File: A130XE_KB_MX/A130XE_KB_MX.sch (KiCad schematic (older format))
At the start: 77 parts, among them J1 34 pin RIBBON KEYBOARD CABLE, J2 Conn_01x02_Male, J3 Conn_01x03_Male, J4 Conn_01x03_Male, SW1 KS_RESET, SW10 K_5, SW11 K_I, SW12 K_T, SW13 K_G, SW14 K_SPACE, SW15 K_B, SW16 K_K, SW17 KS_SELECT, SW18 K_4, SW19 K_O, SW2 K_6, SW20 K_R, SW21 K_F, SW22 K_M, SW23 K_V, SW24 K_L, SW25 K_3, SW26 K_P, SW27 K_E, SW28 K_D, SW29 KS_START, SW3 K_U, SW30 K_comma, SW31 K_comdot, SW32 K_C, SW33 K_dot, SW34 K_2, SW35 K_minus, SW36 K_W, SW37 K_S, SW38 K_X, SW39 K_plus, SW4 K_Y, SW40 K_1, SW41 K_equal, SW42 K_Q, SW43 K_A, SW44 K_slash, SW45 K_asterisk, SW46 K_Z, SW47 K_ATARI, SW48 K_ESC, SW49 K_RETURN, SW5 K_H, SW50 K_TAB, SW51 K_CAPS, SW52 K_CTRL, SW53 K_LSHIFT, SW54 K_RSHIFT, SW55 K_BRK, SW56 K_DEL, SW57 K_GT, SW58 K_LT, SW59 K_0, SW6 K_N, SW60 K_9, SW61 K_8, SW62 K_7, SW63 K_SPACE_1, SW64 K_SPACE_2, SW65 K_F1, SW66 K_F2, SW67 K_F3, SW68 K_F4, SW7 KS_HELP, SW8 K_J, SW9 KS_OPTION

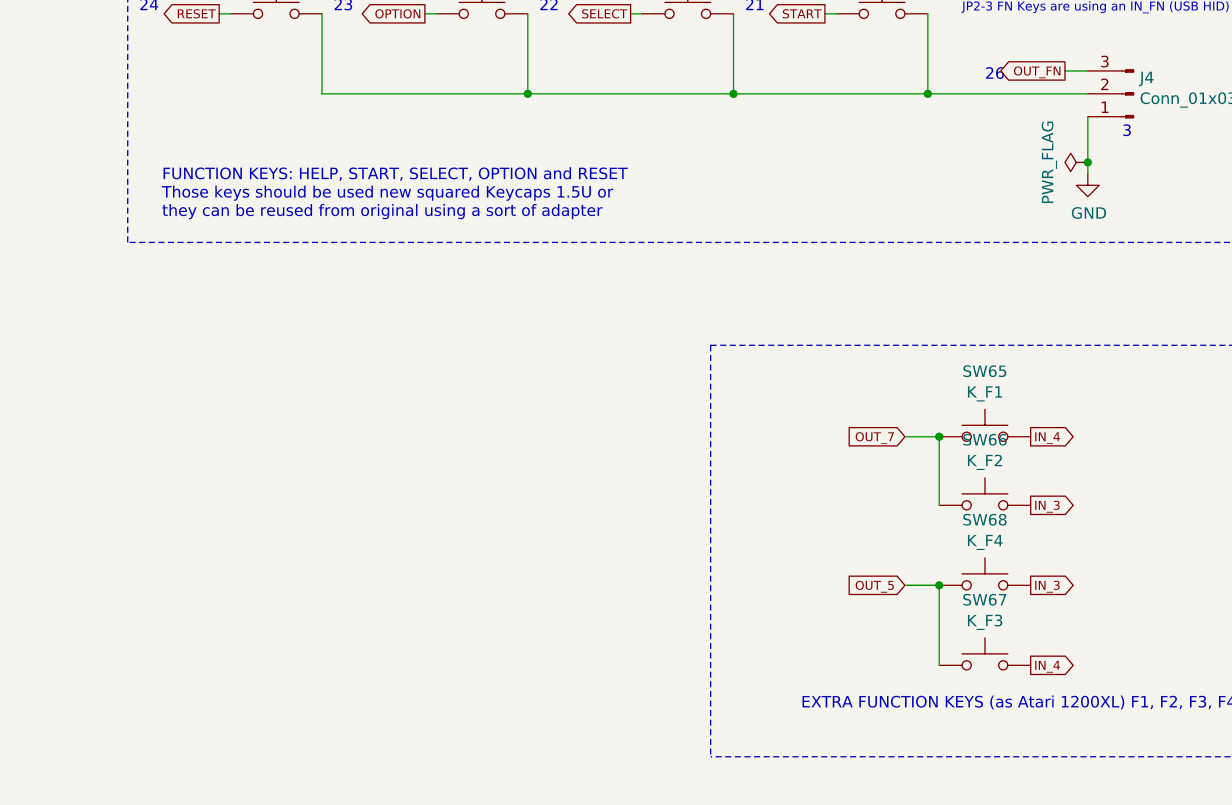
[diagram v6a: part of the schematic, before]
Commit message: Updated some text schematics information
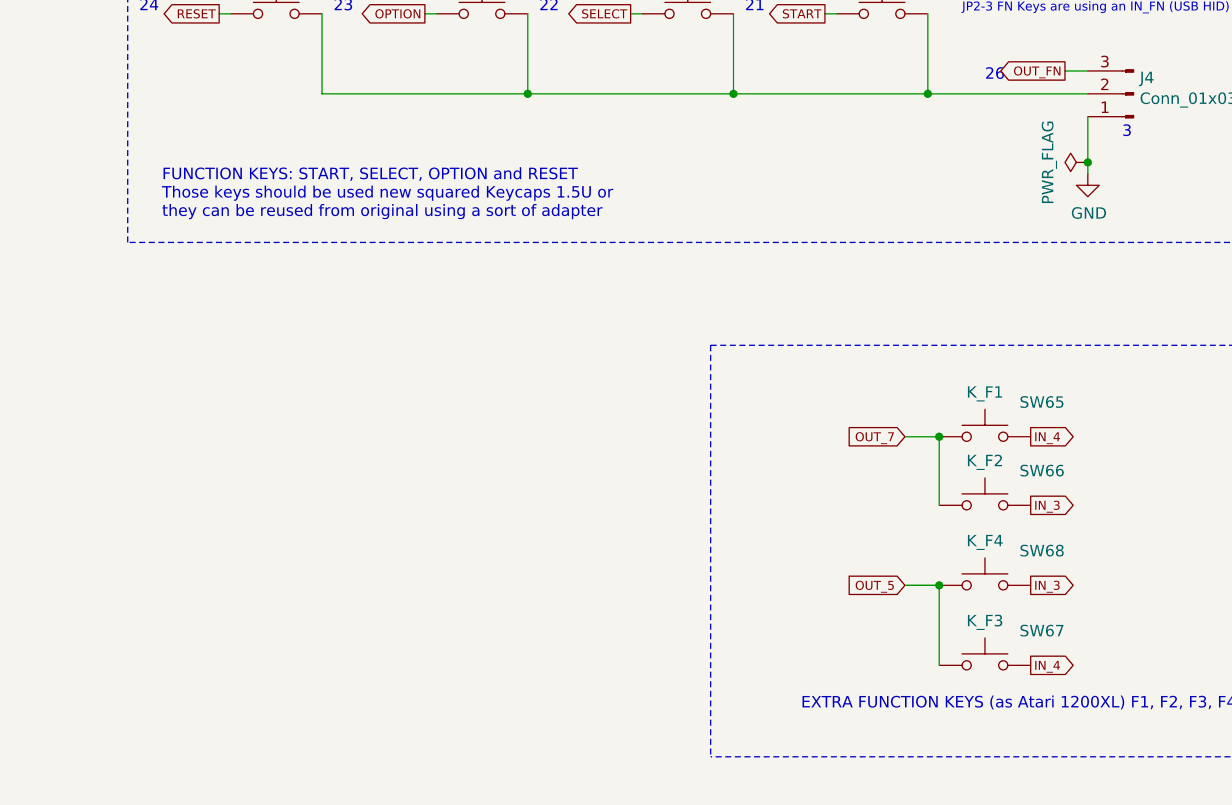
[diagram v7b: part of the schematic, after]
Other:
- note added: "FUNCTION KEYS: START, SELECT, OPTION and RESET\nThose keys should be used new squared Keycaps 1.5U or\nthey can be reused from original using a sort of adapter"
- note removed: "FUNCTION KEYS: HELP, START, SELECT, OPTION and RESET\nThose keys should be used new squared Keycaps 1.5U or\nthey can be reused from original using a sort of adapter"
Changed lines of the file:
@@
 U 1 1 5F8424D3
 P 13800 5000
-F 0 "SW65" H 13800 5285 50  0000 C CNN
+F 0 "SW65" H 14050 5150 50  0000 C CNN
 F 1 "K_F1" H 13800 5194 50  0000 C CNN
 F 2 "RetroBitLab:SW_Cherry_MX1A_1.00u_PCB_3d" H 13800 5200 50  0001 C CNN
@@
 U 1 1 5F8425CB
 P 13800 5300
-F 0 "SW66" H 13800 5585 50  0000 C CNN
+F 0 "SW66" H 14050 5450 50  0000 C CNN
 F 1 "K_F2" H 13800 5494 50  0000 C CNN
 F 2 "RetroBitLab:SW_Cherry_MX1A_1.00u_PCB_3d" H 13800 5500 50  0001 C CNN
@@
 U 1 1 5F842671
 P 13800 6000
-F 0 "SW67" H 13800 6285 50  0000 C CNN
+F 0 "SW67" H 14050 6150 50  0000 C CNN
 F 1 "K_F3" H 13800 6194 50  0000 C CNN
 F 2 "RetroBitLab:SW_Cherry_MX1A_1.00u_PCB_3d" H 13800 6200 50  0001 C CNN
@@
 U 1 1 5F84271F
 P 13800 5650
-F 0 "SW68" H 13800 5935 50  0000 C CNN
+F 0 "SW68" H 14050 5800 50  0000 C CNN
 F 1 "K_F4" H 13800 5844 50  0000 C CNN
 F 2 "RetroBitLab:SW_Cherry_MX1A_1.00u_PCB_3d" H 13800 5850 50  0001 C CNN
@@
 Connection ~ 8150 1400
 Text Notes 10200 4050 0    50   ~ 0
-FUNCTION KEYS: HELP, START, SELECT, OPTION and RESET\nThose keys should be used new squared Keycaps 1.5U or\nthey can be reused from original using a sort of adapter
+FUNCTION KEYS: START, SELECT, OPTION and RESET\nThose keys should be used new squared Keycaps 1.5U or\nthey can be reused from original using a sort of adapter
 Wire Wire Line
 	13300 8650 13310 8650

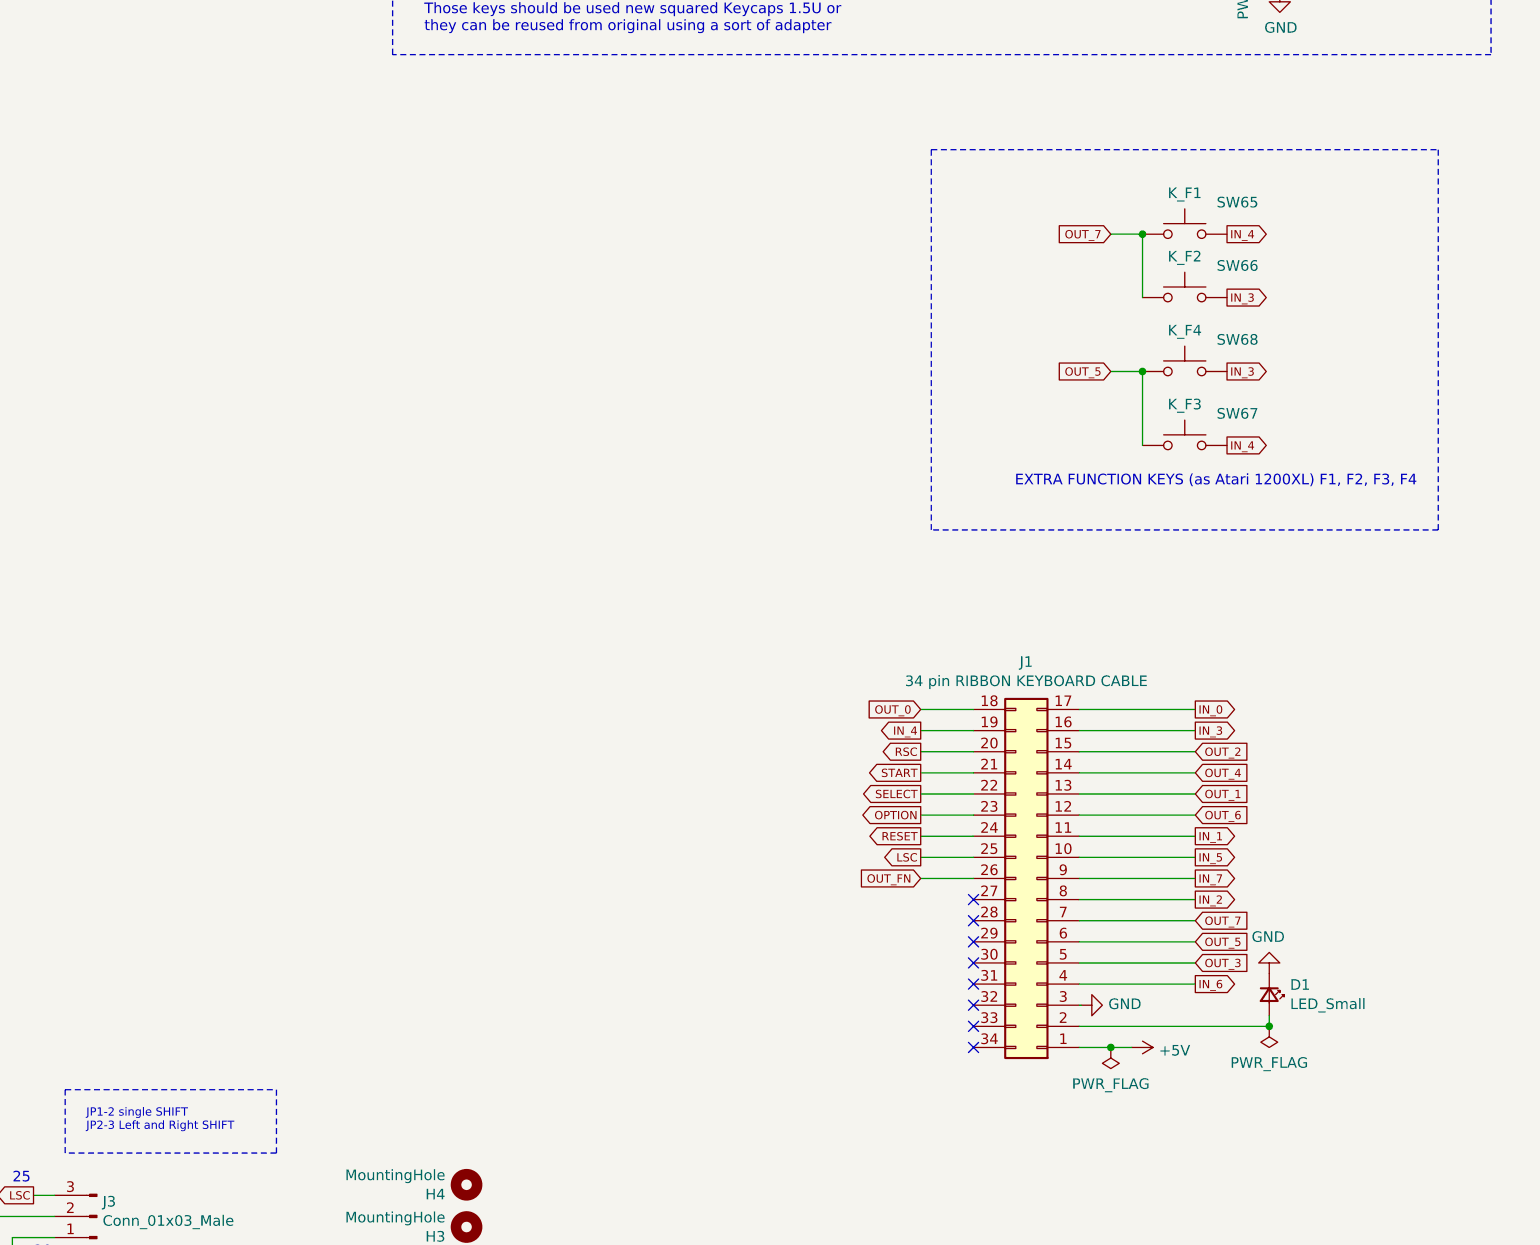
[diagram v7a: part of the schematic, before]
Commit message: New FPC cable. The Flat ribbon is for external USB HID Keyboard
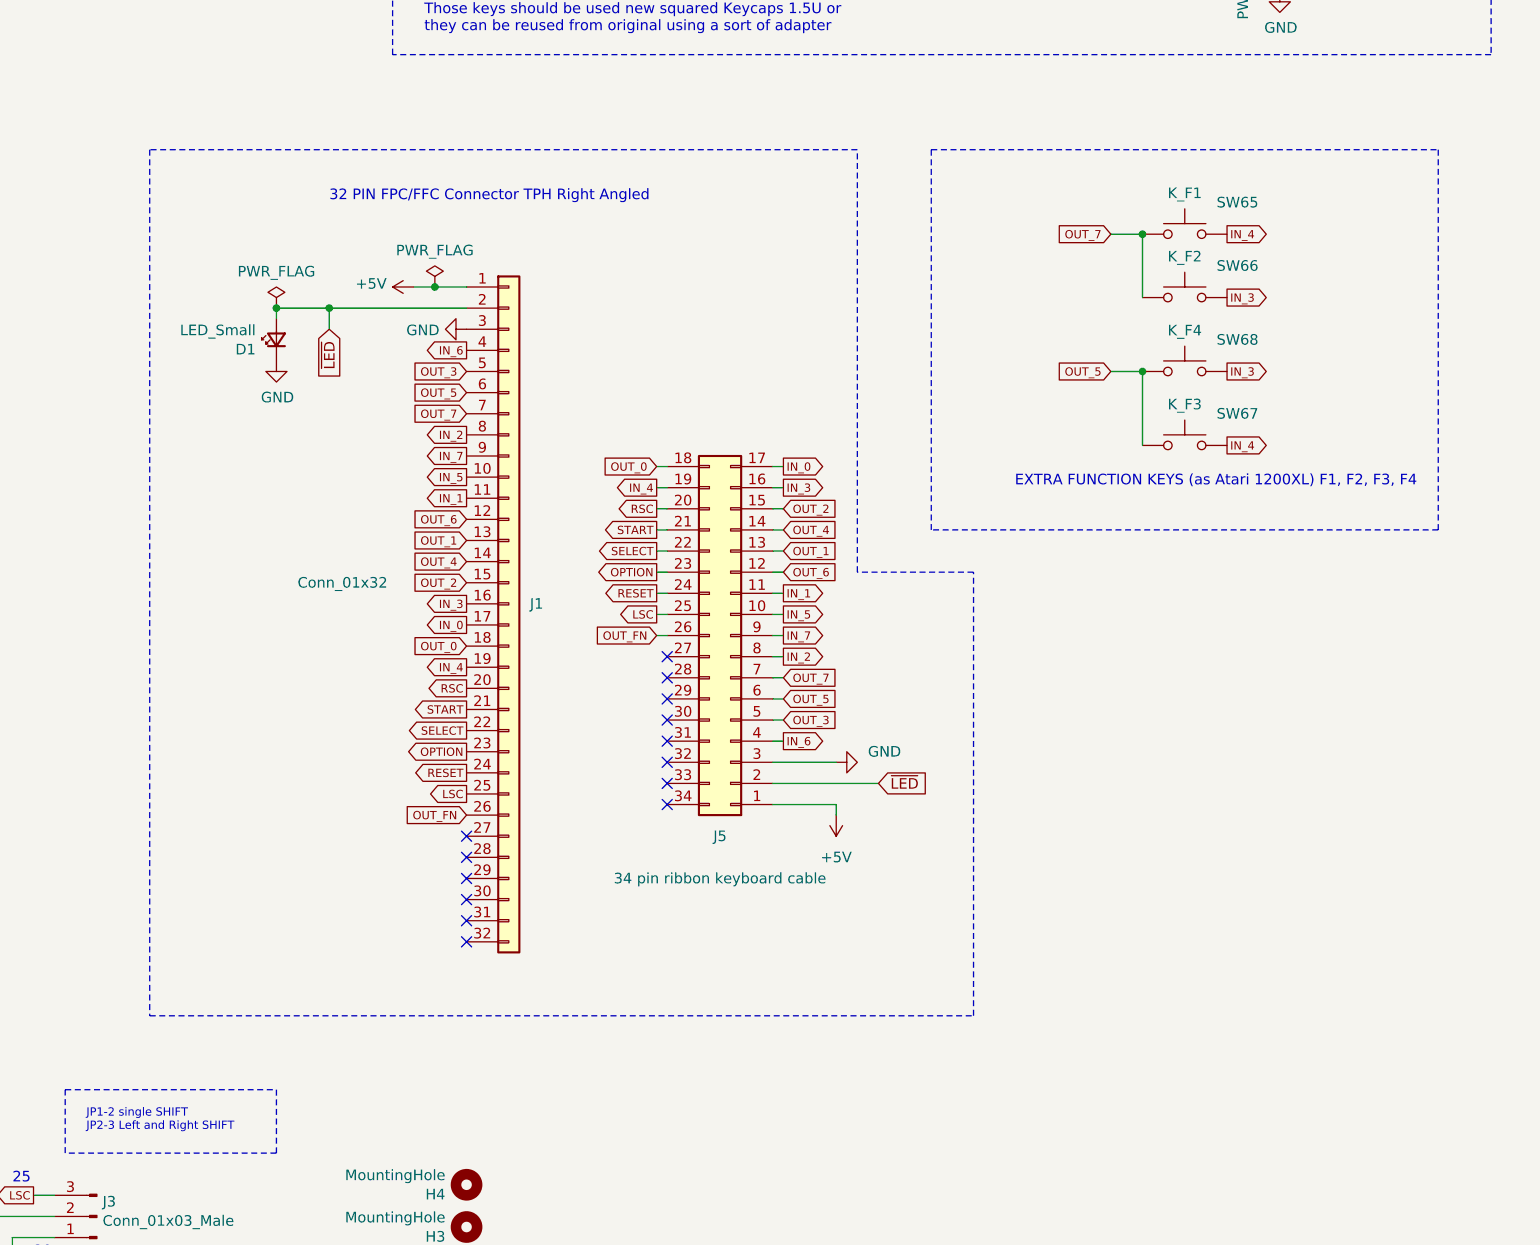
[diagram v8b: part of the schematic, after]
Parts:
- removed J1: 34 pin RIBBON KEYBOARD CABLE, Connector_PinHeader_2.54mm:PinHeader_2x17_P2.54mm_Vertical, symbol Connector_Generic:Conn_02x17_Counter_Clockwise
- added J1: Conn_01x32, RetroBitLab:FFC-1.25mm-RA-5204403245, symbol Connector_Generic:Conn_01x32
- added J5: 34 pin ribbon keyboard cable, Connector_IDC:IDC-Header_2x17_P2.54mm_Vertical, symbol Connector_Generic:Conn_02x17_Counter_Clockwise
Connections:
- net +5V: now also J1.1 (Pin_1), J5.1 (Pin_1)
- net GND: now also J1.3 (Pin_3), J5.3 (Pin_3)
- net IN_0: now also J1.17 (Pin_17), J5.17 (Pin_17)
- net IN_1: now also J1.11 (Pin_11), J5.11 (Pin_11)
- net IN_2: now also J1.8 (Pin_8), J5.8 (Pin_8)
- net IN_3: now also J1.16 (Pin_16), J5.16 (Pin_16)
- net IN_4: now also J1.19 (Pin_19), J5.19 (Pin_19)
- net IN_5: now also J1.10 (Pin_10), J5.10 (Pin_10)
- net IN_6: now also J1.4 (Pin_4), J5.4 (Pin_4)
- net IN_7: now also J1.9 (Pin_9), J5.9 (Pin_9)
- net LSC: now also J1.25 (Pin_25), J5.25 (Pin_25)
- net OPTION: now also J1.23 (Pin_23), J5.23 (Pin_23)
- net OUT_0: now also J1.18 (Pin_18), J5.18 (Pin_18)
- net OUT_1: now also J1.13 (Pin_13), J5.13 (Pin_13)
- net OUT_2: now also J1.15 (Pin_15), J5.15 (Pin_15)
- net OUT_3: now also J1.5 (Pin_5), J5.5 (Pin_5)
- net OUT_4: now also J1.14 (Pin_14), J5.14 (Pin_14)
- net OUT_5: now also J1.6 (Pin_6), J5.6 (Pin_6)
- net OUT_6: now also J1.12 (Pin_12), J5.12 (Pin_12)
- net OUT_7: now also J1.7 (Pin_7), J5.7 (Pin_7)
- net OUT_FN: now also J1.26 (Pin_26), J5.26 (Pin_26)
- net RESET: now also J1.24 (Pin_24), J5.24 (Pin_24)
- net RSC: now also J1.20 (Pin_20), J5.20 (Pin_20)
- net SELECT: now also J1.22 (Pin_22), J5.22 (Pin_22)
- net START: now also J1.21 (Pin_21), J5.21 (Pin_21)
- net ~LED: now reaches D1.2 (A)
- net ~LED: now also J1.2 (Pin_2), J5.2 (Pin_2)
- no-connect marks 8 -> 14
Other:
- note added: "32 PIN FPC/FFC Connector TPH Right Angled"
- moved on the sheet: D1
